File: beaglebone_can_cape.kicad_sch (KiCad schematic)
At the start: 26 parts, among them J1 Conn_01x02_Pin, J2 Conn_01x02_Pin, J3 DTM15-12PA, J4 Conn_02x02_Top_Bottom, J5 Battery Harness, P8 BeagleBone_Black_Header, P9 BeagleBone_Black_Header, U1 TCAN332, U2 TCAN332, U3 LMR51430

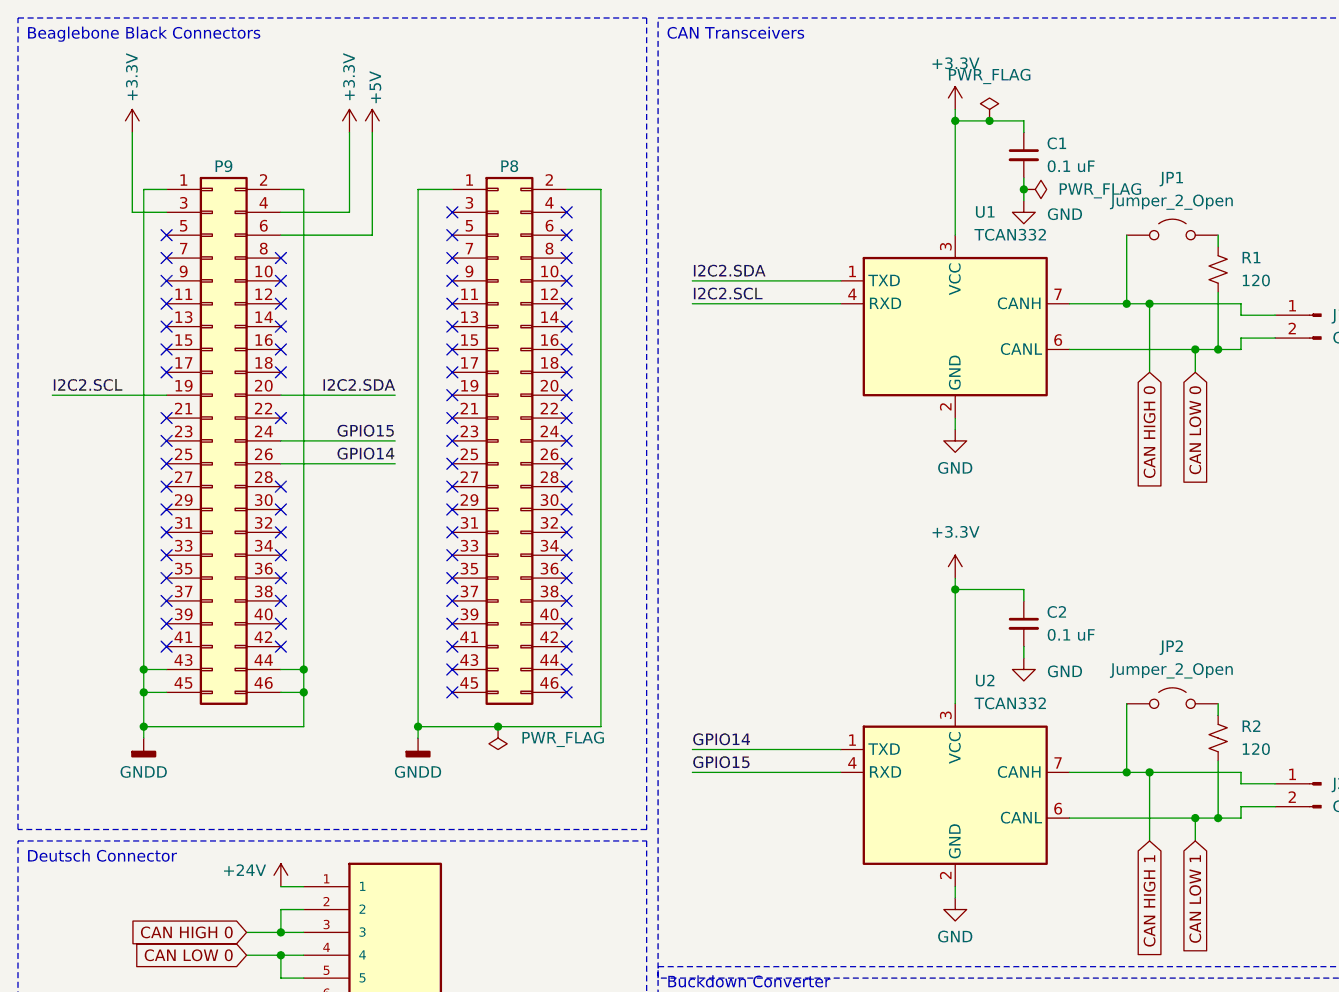
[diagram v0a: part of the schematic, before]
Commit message: Before-Meeting final PCB and Schematic changes
* Redid the battery circuit to be... yk... correct because I wired it wrong the first time lols
* I changed the width of all high voltage & current lines to 0.8mm, really no big change there, nothing had to be moved
* Looked in depth at anything missing, I think we're just about good to go
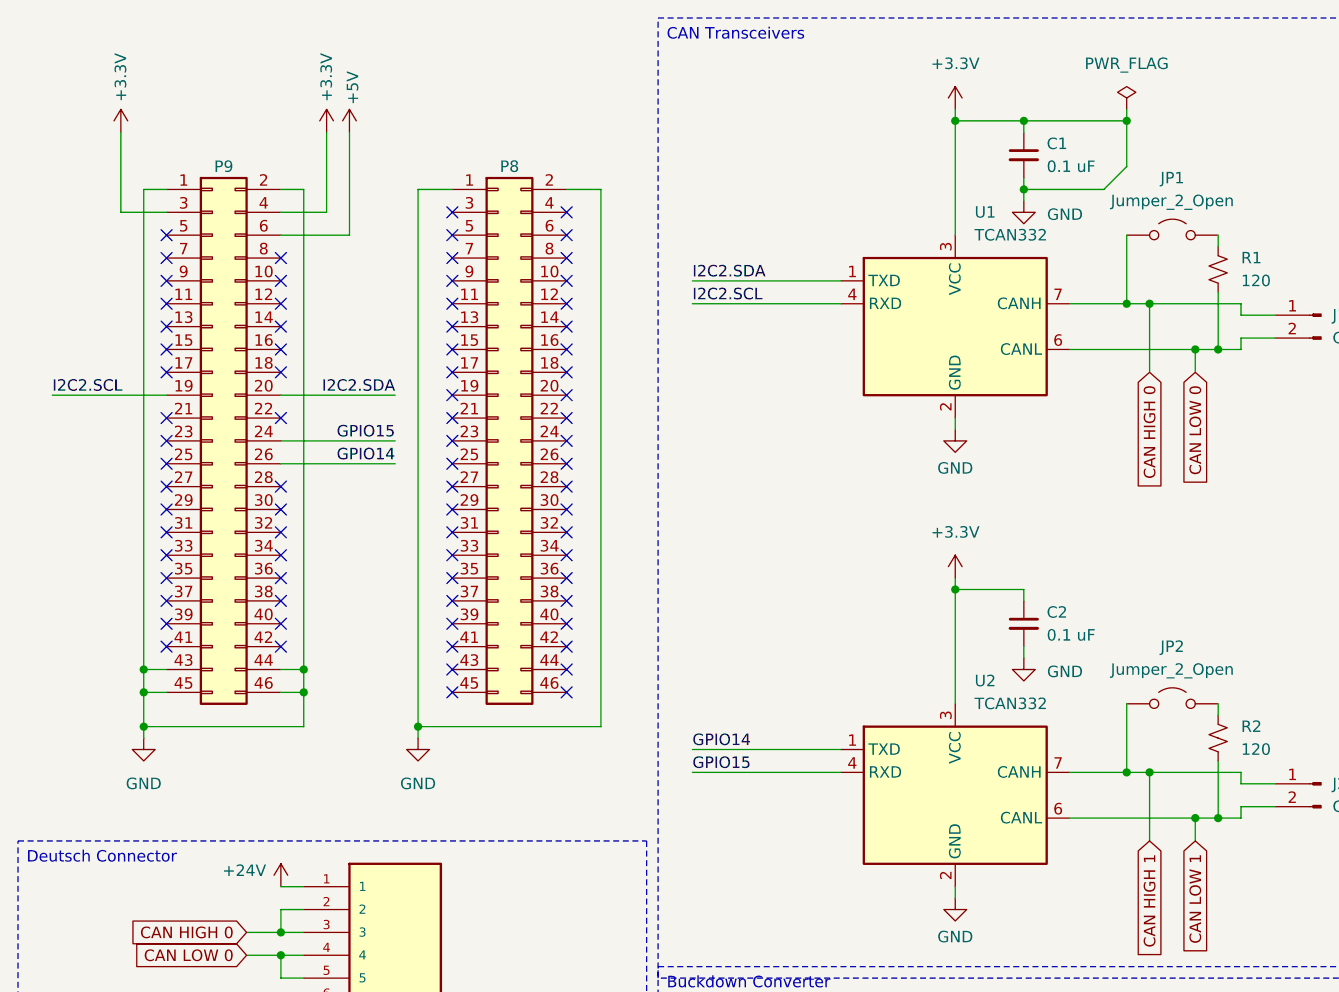
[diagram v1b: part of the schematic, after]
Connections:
- net GND is gone; now on net +3.3V: C1.2, C2.2, Cin1.2, Cout1.2, D1.2 (A), J3.11, J3.12, J3.6, R4.2, U1.2 (GND), U2.2 (GND), U3.1 (GND)
- net GNDD is gone; now on net +3.3V: P8.1 (Pin_1), P8.2 (Pin_2), P9.1 (Pin_1), P9.2 (Pin_2), P9.43 (Pin_43), P9.44 (Pin_44), P9.45 (Pin_45), P9.46 (Pin_46)

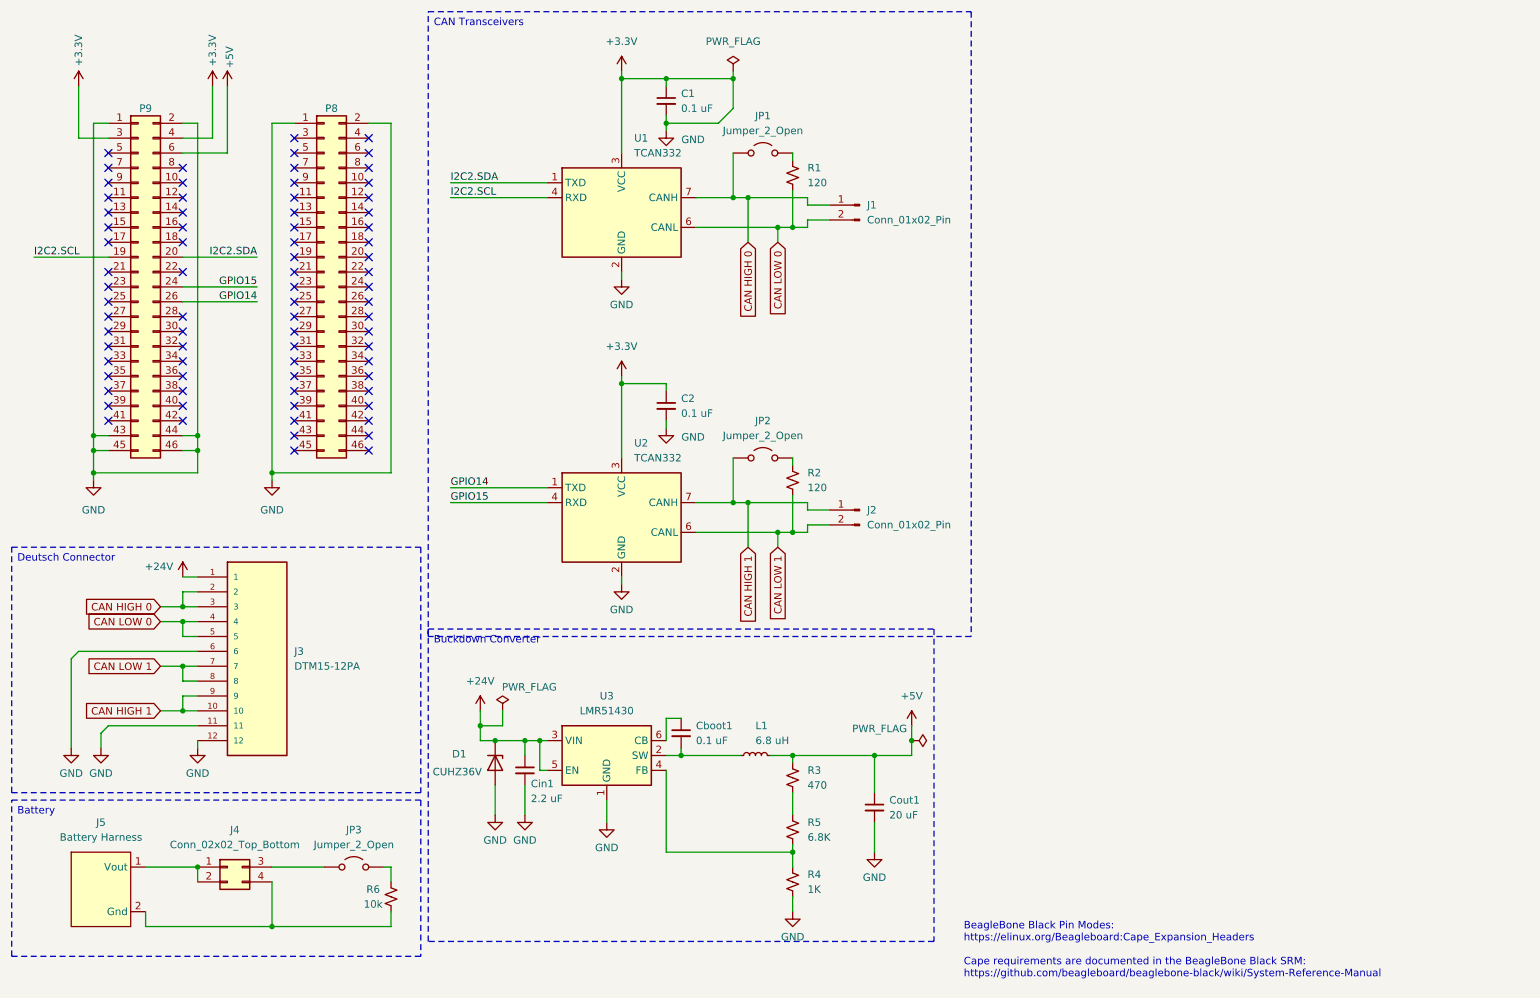
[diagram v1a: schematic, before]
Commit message: Joey request LED + battery harness things
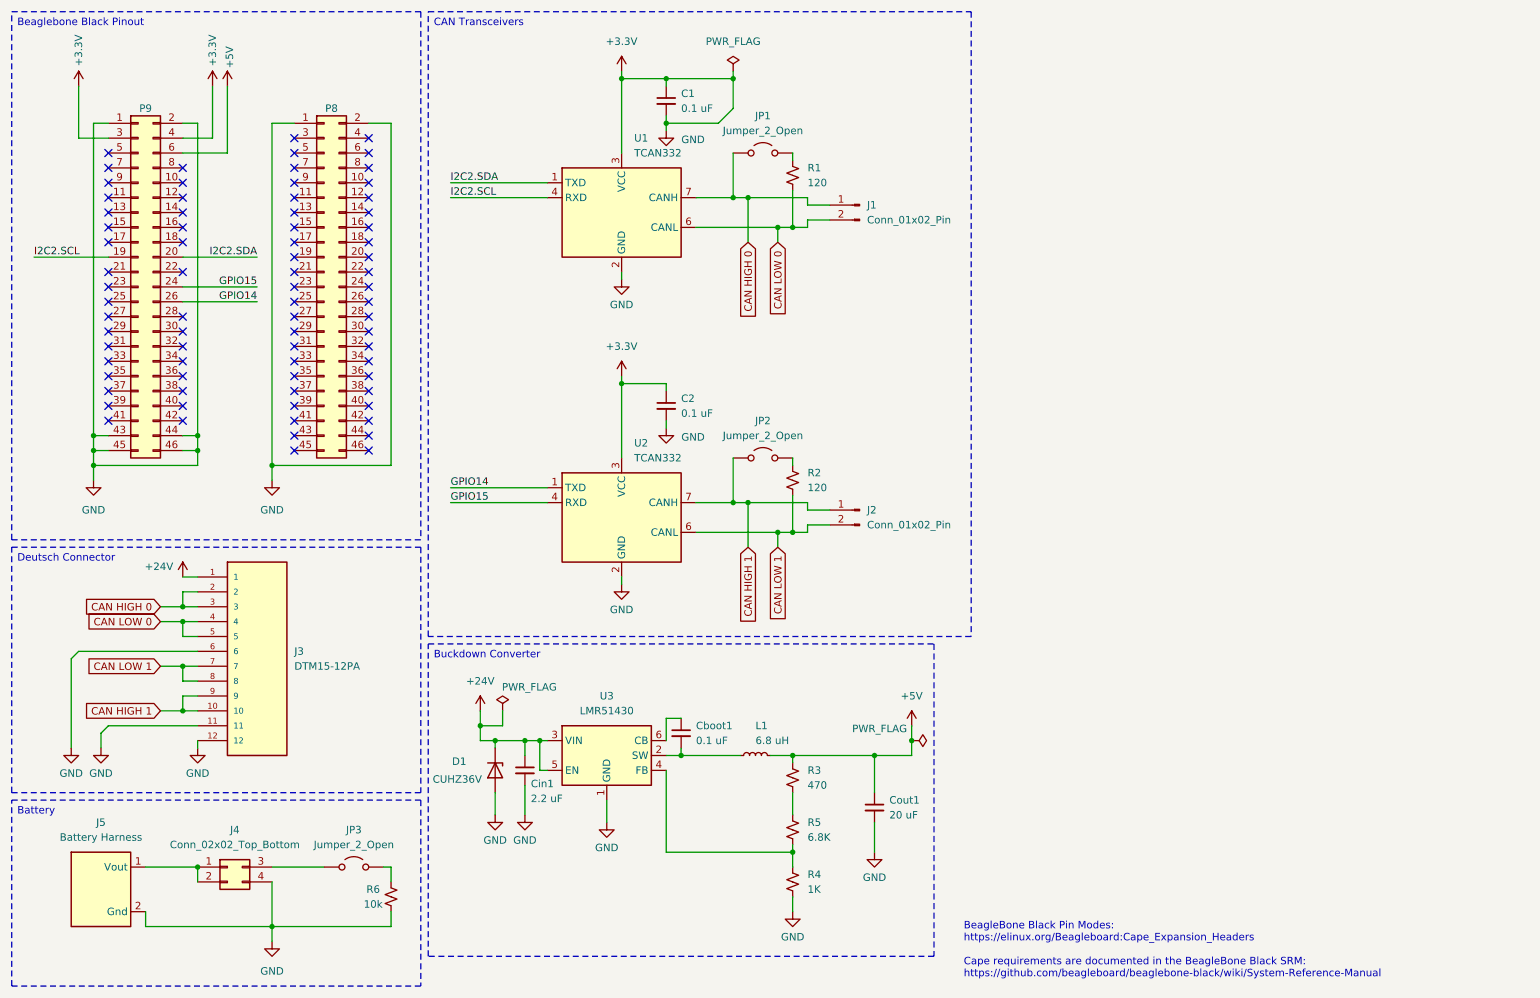
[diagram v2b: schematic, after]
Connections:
- net +3.3V: now also J4.4 (Pin_4), J5.2 (Gnd), R6.2
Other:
- moved on the sheet: D1
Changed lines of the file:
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@@
 		)
 	)
-	(text_box "Buckdown Converter\n"
+	(text_box "Beaglebone Black Pinout"
 		(exclude_from_sim no)
-		(at 86.36 120.65 0)
-		(size 86.36 53.34)
+		(at 15.24 15.24 0)
+		(size 69.85 90.17)
 		(margins 0.9525 0.9525 0.9525 0.9525)
 		(stroke
@@
 		)
 	)
+	(text_box "Buckdown Converter\n"
+		(exclude_from_sim no)
+		(at 86.36 123.19 0)
+		(size 86.36 53.34)
+		(margins 0.9525 0.9525 0.9525 0.9525)
+		(stroke
+			(width 0)
+			(type dash)
+		)
+		(fill
+			(type none)
+		)
+		(effects
+			(font
+				(size 1.27 1.27)
+			)
+			(justify left top)
+		)
+	)
 	(text_box "Battery\n"
 		(exclude_from_sim no)
 		(at 15.24 149.86 0)
-		(size 69.85 26.67)
+		(size 69.85 31.75)
 		(margins 0.9525 0.9525 0.9525 0.9525)
 		(stroke
@@
 	)
 	(junction
-		(at 29.21 93.98)
-		(diameter 0)
-		(color 0 0 0 0)
-	)
-	(junction
 		(at 44.45 116.84)
 		(diameter 0)
@@
 	)
 	(junction
-		(at 59.69 93.98)
+		(at 29.21 92.71)
 		(diameter 0)
 		(color 0 0 0 0)
@@
 	)
 	(junction
+		(at 59.69 92.71)
+		(diameter 0)
+		(color 0 0 0 0)
+	)
+	(junction
 		(at 148.59 158.75)
 		(diameter 0)
@@
 	(wire
 		(pts
-			(xy 29.21 93.98) (xy 29.21 95.25)
-		)
-		(stroke
-			(width 0)
-			(type default)
-		)
-	)
-	(wire
-		(pts
 			(xy 102.87 139.7) (xy 105.41 139.7)
 		)
@@
 	(wire
 		(pts
-			(xy 59.69 93.98) (xy 80.01 93.98)
+			(xy 59.69 92.71) (xy 80.01 92.71)
 		)
 		(stroke
@@
 	(wire
 		(pts
+			(xy 59.69 92.71) (xy 59.69 95.25)
+		)
+		(stroke
+			(width 0)
+			(type default)
+		)
+	)
+	(wire
+		(pts
 			(xy 151.13 50.8) (xy 151.13 52.07)
 		)
@@
 	(wire
 		(pts
+			(xy 59.69 171.45) (xy 59.69 173.99)
+		)
+		(stroke
+			(width 0)
+			(type default)
+		)
+	)
+	(wire
+		(pts
 			(xy 44.45 64.77) (xy 57.15 64.77)
 		)
@@
 	(wire
 		(pts
-			(xy 97.79 147.32) (xy 97.79 152.4)
+			(xy 97.79 148.59) (xy 97.79 152.4)
 		)
 		(stroke
@@
 	(wire
 		(pts
+			(xy 97.79 140.97) (xy 97.79 139.7)
+		)
+		(stroke
+			(width 0)
+			(type default)
+		)
+	)
+	(wire
+		(pts
 			(xy 140.97 46.99) (xy 151.13 46.99)
 		)
@@
 	(wire
 		(pts
-			(xy 29.21 90.17) (xy 29.21 93.98)
+			(xy 29.21 90.17) (xy 29.21 92.71)
 		)
 		(stroke
@@
 	(wire
 		(pts
-			(xy 59.69 34.29) (xy 59.69 93.98)
+			(xy 59.69 34.29) (xy 59.69 92.71)
 		)
 		(stroke
@@
 	(wire
 		(pts
-			(xy 59.69 93.98) (xy 59.69 95.25)
-		)
-		(stroke
-			(width 0)
-			(type default)
-		)
-	)
-	(wire
-		(pts
 			(xy 44.45 90.17) (xy 46.99 90.17)
 		)
@@
 	(wire
 		(pts
-			(xy 46.99 93.98) (xy 29.21 93.98)
+			(xy 46.99 92.71) (xy 29.21 92.71)
 		)
 		(stroke
@@
 	(wire
 		(pts
+			(xy 29.21 92.71) (xy 29.21 95.25)
+		)
+		(stroke
+			(width 0)
+			(type default)
+		)
+	)
+	(wire
+		(pts
 			(xy 44.45 134.62) (xy 46.99 134.62)
 		)
@@
 	(wire
 		(pts
-			(xy 80.01 93.98) (xy 80.01 34.29)
+			(xy 80.01 92.71) (xy 80.01 34.29)
 		)
 		(stroke
@@
 	(wire
 		(pts
-			(xy 46.99 90.17) (xy 46.99 93.98)
+			(xy 46.99 90.17) (xy 46.99 92.71)
 		)
 		(stroke
@@
 	(symbol
 		(lib_id "Diode:PTVS5V0Z1USK")
-		(at 97.79 143.51 270)
+		(at 97.79 144.78 270)
 		(unit 1)
 		(exclude_from_sim no)
@@
 		(dnp no)
 		(property "Reference" "D1"
-			(at 90.424 141.986 90)
+			(at 90.424 143.256 90)
 			(effects
 				(font
@@
 		)
 		(property "Value" "CUHZ36V"
-			(at 87.122 145.034 90)
+			(at 87.122 146.304 90)
 			(effects
 				(font
@@
 		)
 		(property "Footprint" "SeniorDesign:TVSDiode"
-			(at 93.345 143.51 0)
+			(at 93.345 144.78 0)
 			(effects
 				(font
@@
 		)
 		(property "Datasheet" "https://toshiba.semicon-storage.com/info/CUHZ36V_datasheet_en_20210917.pdf?did=70664&prodName=CUHZ36V"
-			(at 97.79 143.51 0)
+			(at 97.79 144.78 0)
 			(effects
 				(font
@@
 		)
 		(property "Description" ""
-			(at 97.79 143.51 0)
+			(at 97.79 144.78 0)
 			(effects
 				(font
@@
 					(unit 1)
 				)
+			)
+		)
+	)
+	(symbol
+		(lib_id "power:GND")
+		(at 59.69 173.99 0)
+		(unit 1)
+		(exclude_from_sim no)
+		(in_bom yes)
+		(on_board yes)
+		(dnp no)
+		(fields_autoplaced yes)
+		(property "Reference" "#PWR023"
+			(at 59.69 180.34 0)
+			(effects
+				(font
+					(size 1.27 1.27)
+				)
+				(hide yes)
+			)
+		)
+		(property "Value" "GND"
+			(at 59.69 179.07 0)
+			(effects
+				(font
+					(size 1.27 1.27)
+				)
+			)
+		)
+		(property "Footprint" ""
+			(at 59.69 173.99 0)
+			(effects
+				(font
+					(size 1.27 1.27)
+				)
+				(hide yes)
+			)
+		)
+		(property "Datasheet" ""
+			(at 59.69 173.99 0)
+			(effects
+				(font
+					(size 1.27 1.27)
+				)
+				(hide yes)
+			)
+		)
+		(property "Description" "Power symbol creates a global label with name \"GND\" , ground"
+			(at 59.69 173.99 0)
+			(effects
+				(font
+					(size 1.27 1.27)
+				)
+				(hide yes)
+			)
+		)
+		(pin "1"
+		)
+		(instances
+			(project ""
+				(path "/e63e39d7-6ac0-4ffd-8aa3-1841a4541b55"
+					(reference "#PWR023")
+					(unit 1)
+				)

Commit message: pushing changes
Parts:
- added D2: CAN0LED, LED_SMD:LED_0805_2012Metric, symbol Device:LED
- added D3: CAN1LED, LED_SMD:LED_0805_2012Metric, symbol Device:LED
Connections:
- net +3.3V: no longer C1.2, C2.2, Cin1.2, Cout1.2, D1.2 (A), J3.11, J3.12, J3.6, J4.4 (Pin_4), J5.2 (Gnd), P8.1 (Pin_1), P8.2 (Pin_2), P9.1 (Pin_1), P9.2 (Pin_2), P9.43 (Pin_43), P9.44 (Pin_44), P9.45 (Pin_45), P9.46 (Pin_46), R4.2, R6.2, U1.2 (GND), U2.2 (GND), U3.1 (GND)
- net GPIO3: now reaches P9.21 (Pin_21)
- net GPIO3: now also D3.2 (A)
- net GPIO2: now reaches P9.22 (Pin_22)
- net GPIO2: now also D2.2 (A)
- new net GND: C1.2, C2.2, Cin1.2, Cout1.2, D1.2 (A), D2.1 (K), D3.1 (K), J3.11, J3.12, J3.6, J4.4 (Pin_4), J5.2 (Gnd), P8.1 (Pin_1), P8.2 (Pin_2), P9.1 (Pin_1), P9.2 (Pin_2), P9.43 (Pin_43), P9.44 (Pin_44), P9.45 (Pin_45), P9.46 (Pin_46), R4.2, R6.2, U1.2 (GND), U2.2 (GND), U3.1 (GND)
- no-connect marks 77 -> 75
